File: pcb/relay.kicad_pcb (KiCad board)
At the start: 2 copper layers, 22 parts, among them IC1 ATTINY13-P, P1 CONN_01X02, P2 CONN_02X20, Q1 BC548, Q2 BC548, SW1 SW_PUSH, U1 MC78L05ACP, U2 DX_MODULE

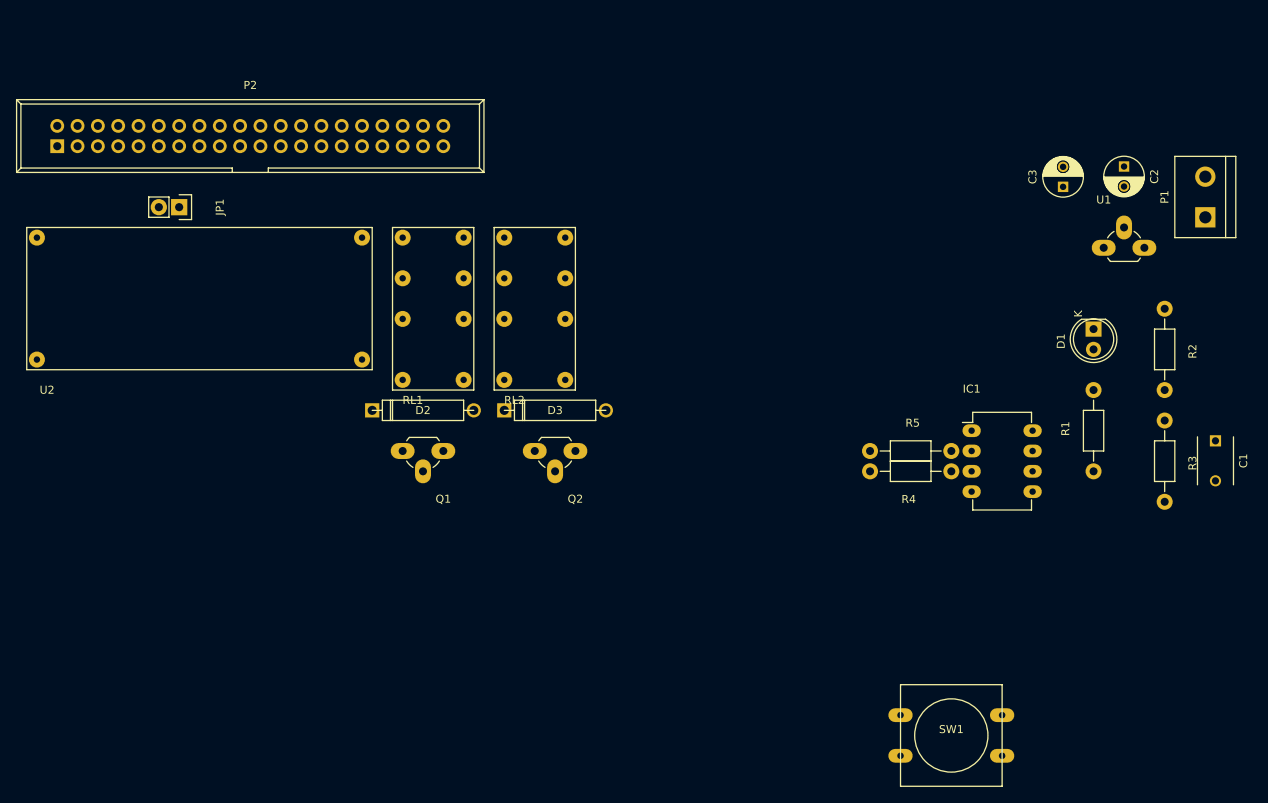
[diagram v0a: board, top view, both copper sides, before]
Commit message: Final version of PCB sent to OSHPark.
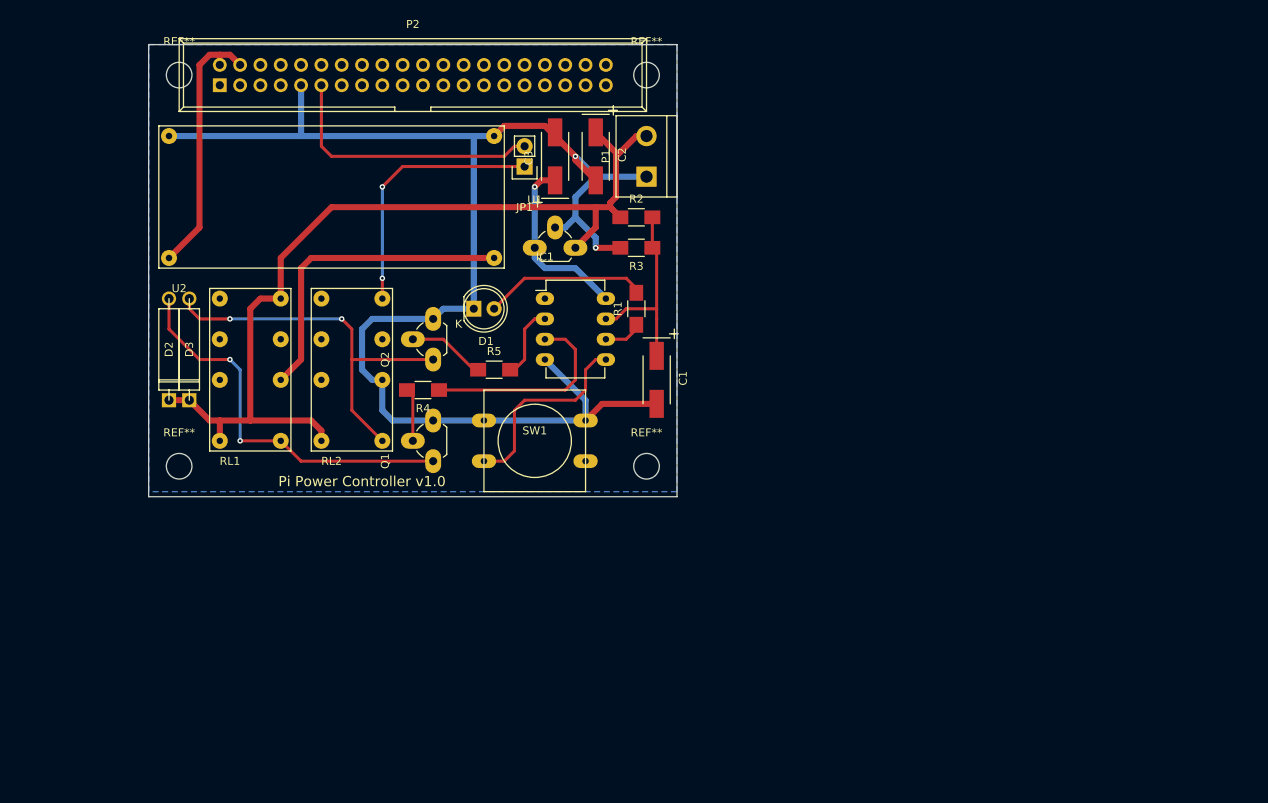
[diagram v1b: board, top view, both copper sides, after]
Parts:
- added REF**: MountingHole_3.2mm_M3, Mounting_Holes:MountingHole_3.2mm_M3, F.Cu at (41.9, 44.5)
- added REF**: MountingHole_3.2mm_M3, Mounting_Holes:MountingHole_3.2mm_M3, F.Cu at (100.3, 44.5)
- added REF**: MountingHole_3.2mm_M3, Mounting_Holes:MountingHole_3.2mm_M3, F.Cu at (41.9, 93.3)
- added REF**: MountingHole_3.2mm_M3, Mounting_Holes:MountingHole_3.2mm_M3, F.Cu at (100.3, 93.3)
- C1: value C -> 22uF; footprint Capacitors_ThroughHole:C_Disc_D6_P5 -> Capacitors_Tantalum_SMD:TantalC_SizeC_EIA-6032_HandSoldering
- C2, C3: value 1uF -> 22uF; footprint Capacitors_ThroughHole:C_Radial_D5_L11_P2.5 -> Capacitors_Tantalum_SMD:TantalC_SizeC_EIA-6032_HandSoldering
- R1, R2, R3, R4, R5: footprint Resistors_ThroughHole:Resistor_Horizontal_RM10mm -> Resistors_SMD:R_1206_HandSoldering
- moved D1 77.5 mm to (78.7, 73.7), turned to 0 degrees
- moved U1 71.1 mm to (86.4, 66.0)
- moved C1 70.3 mm to (101.6, 82.5)
- moved P1 70.0 mm to (100.3, 54.6)
- moved R3 69.5 mm to (99.1, 66.0), turned to 180 degrees
- moved R2 67.0 mm to (99.1, 62.2), turned to 0 degrees
- moved R4 66.8 mm to (72.4, 83.8)
- moved C2 66.1 mm to (94.0, 54.6)
- moved SW1 63.8 mm to (86.4, 90.2)
- moved C3 63.6 mm to (88.9, 54.6)
- moved R1 60.7 mm to (99.1, 73.7)
- moved IC1 55.8 mm to (87.6, 72.4)
- moved R5 48.1 mm to (81.3, 81.3)
- moved D3 46.4 mm to (43.2, 78.7), turned to 270 degrees
- moved JP1 43.5 mm to (85.1, 55.9), turned to 180 degrees
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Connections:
- C2 pad 2: Net-(C2-Pad2) -> GNDD
- C3 pad 2: Net-(C2-Pad2) -> GNDD
- P1 pad 1: Net-(C2-Pad2) -> GNDD
- U1 pad 2: Net-(C2-Pad2) -> GNDD
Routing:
- net GNDD: track 0.00 -> 184.6 mm, vias 0 -> 2
- net +12V: track 0.00 -> 115.7 mm
- net Net-(D2-Pad2): track 0.00 -> 48.9 mm, vias 0 -> 2
- net Net-(D3-Pad2): track 0.00 -> 48.4 mm, vias 0 -> 2
- net Net-(RL1-Pad8): track 0.00 -> 39.7 mm
- net Net-(JP1-Pad2): track 0.00 -> 34.1 mm
- net Net-(P2-Pad2): track 0.00 -> 33.1 mm
- net Net-(JP1-Pad1): track 0.00 -> 32.8 mm, vias 0 -> 2
- net Net-(IC1-Pad3): track 0.00 -> 25.7 mm
- net Net-(IC1-Pad5): track 0.00 -> 25.0 mm
- net Net-(C1-Pad1): track 0.00 -> 24.4 mm
- net +5VD: track 0.00 -> 22.8 mm, vias 0 -> 1
- net Net-(D1-Pad2): track 0.00 -> 20.4 mm
- net Net-(Q2-Pad2): track 0.00 -> 9.74 mm
- net Net-(IC1-Pad2): track 0.00 -> 9.21 mm
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- added copper zone on B.Cu, net GNDD
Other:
- board outline added: 66 x 56.5 mm
- net class Default: clearance 0.2 -> 0.381; trace_width 0.25 -> 0.381; via_dia 0.6 -> 0.6858; via_drill 0.4 -> 0.3302
- net class GND added: clearance 0.381, trace_width 0.762, via_dia 0.6858, via_drill 0.3302
- net class Power added: clearance 0.381, trace_width 0.762, via_dia 0.6858, via_drill 0.3302
- rule trace_clearance: 0.2 -> 0.381
- rule trace_min: 0.2 -> 0.1524
- rule via_min_drill: 0.3 -> 0.3302
- rule via_min_size: 0.4 -> 0.6858
- board text added: "Pi Power Controller v1.0"
